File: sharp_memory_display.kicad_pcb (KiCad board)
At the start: 2 copper layers, 34.2 x 22.4 mm, 20 parts, among them J1 Conn_01x05, J2 Conn_01x10, J3 Conn_01x05_Male, J4 Conn_01x10

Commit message: simplified version
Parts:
- removed H1, H2, H3, H4: MountingHole, MountingHole:MountingHole_2.2mm_M2_DIN965_Pad
- removed J4: Conn_01x10, Connector_FFC-FPC:Hirose_FH12-10S-0.5SH_1x10-1MP_P0.50mm_Horizontal
- removed REF** (x4): breakaway-mousebites-three, Keebio-Parts:breakaway-mousebites-three
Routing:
- net EXTMODE: track 24.9 -> 9.01 mm, vias 3 -> 2
- net VSSA: track 26.6 -> 11.0 mm, vias 1 -> 0
- net VDDA: track 27.1 -> 12.1 mm, vias 1 -> 0
- net DISP: track 20.5 -> 6.77 mm, vias 1 -> 0
- net EXTCOMIN: track 21.2 -> 8.33 mm, vias 1 -> 0
- net SCLK: track 33.2 -> 26.5 mm, vias 1 -> 0
- net SCS: track 31.5 -> 25.6 mm, vias 1 -> 0
- net VDD: track 46.8 -> 42.9 mm
- net VSS: track 48.3 -> 44.5 mm
- net SI: track 39.5 -> 36.0 mm
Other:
- board size 34.2 x 22.4 mm -> 34.2 x 14 mm

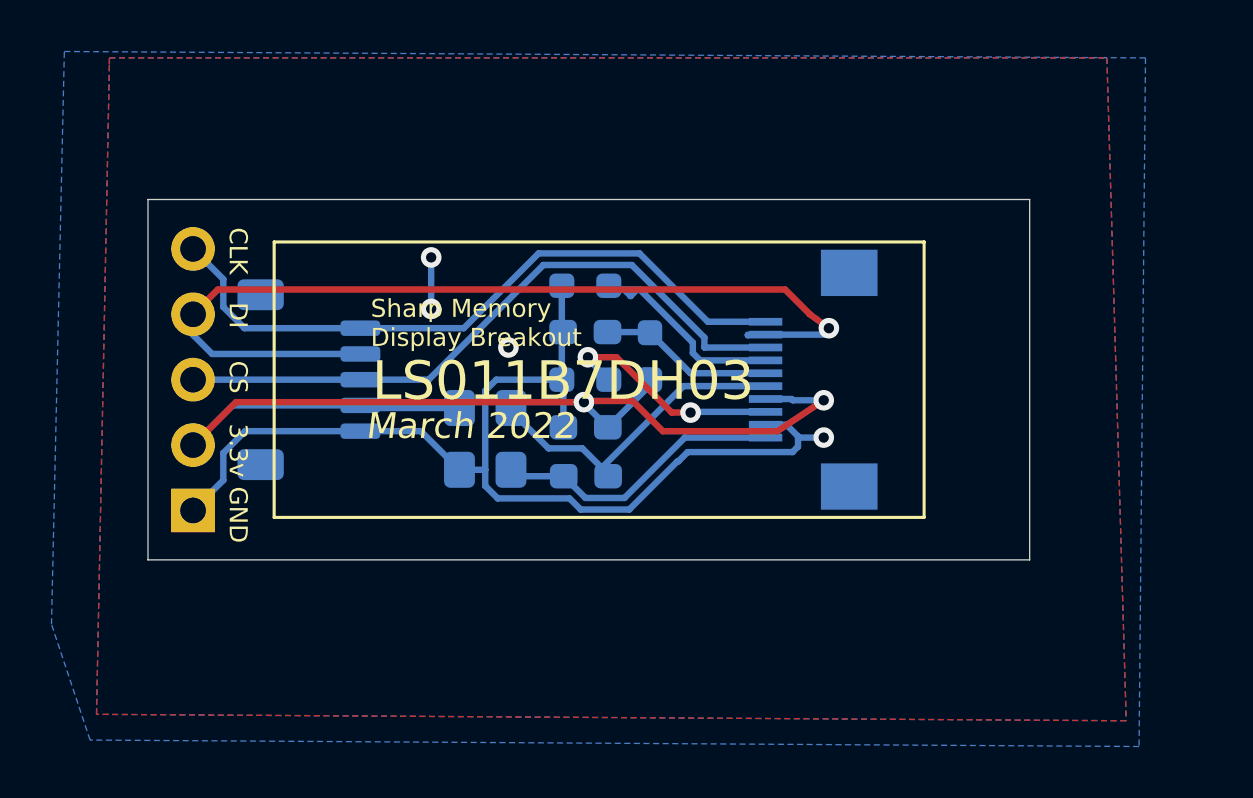
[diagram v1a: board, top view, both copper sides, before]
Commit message: add two extra pint sockets
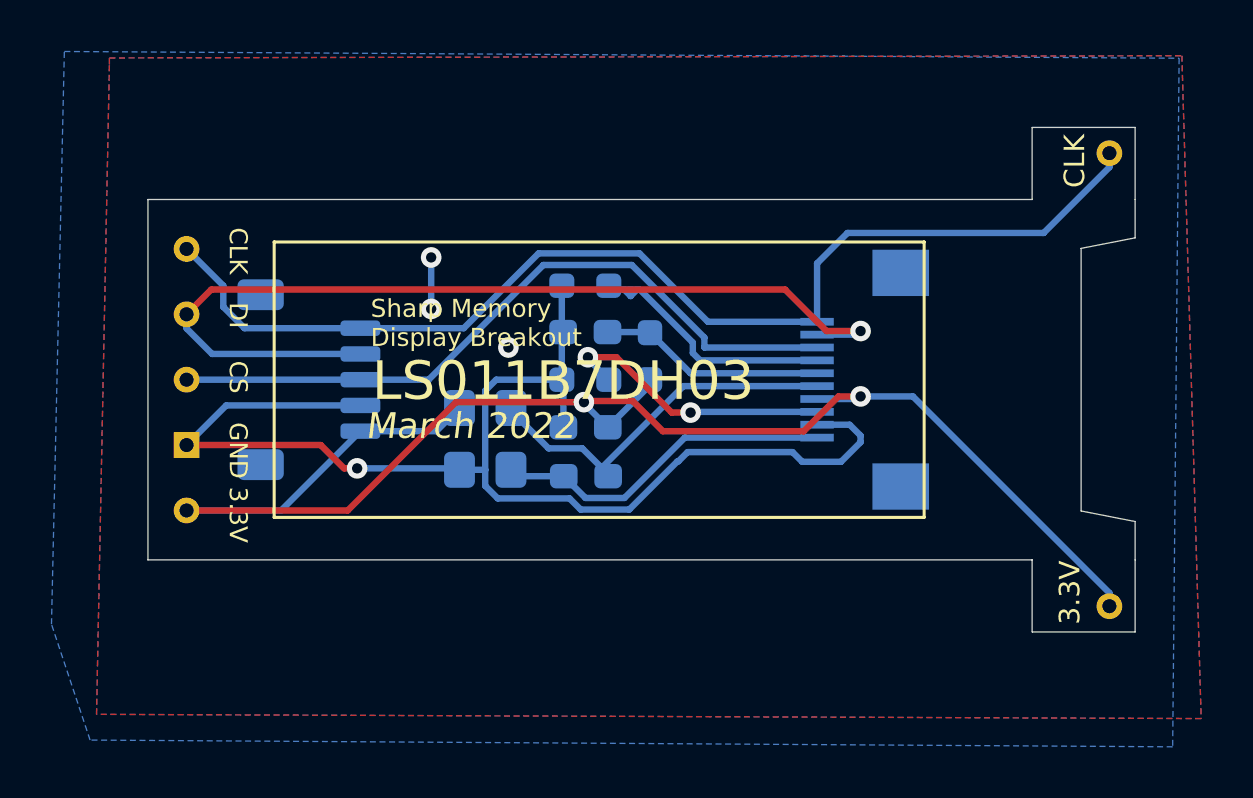
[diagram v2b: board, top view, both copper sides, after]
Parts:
- added J4: Conn_01x01_Female, Connector_PinSocket_2.54mm:PinSocket_1x01_P2.54mm_Vertical, F.Cu at (59.9, 21.7)
- added J5: Conn_01x01_Female, Connector_PinSocket_2.54mm:PinSocket_1x01_P2.54mm_Vertical, F.Cu at (59.9, 39.3)
- moved J2 2.00 mm to (54.9, 30.5)
- moved J1 0.25 mm to (24.0, 35.6)
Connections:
- J1 pad 1: VSS -> VDD
- J1 pad 2: VDD -> VSS
- J3 pad 1: VSS -> VDD
- J3 pad 2: VDD -> VSS
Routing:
- net SCLK: track 26.5 -> 44.3 mm
- net VDD: track 42.9 -> 60.0 mm
- net VSS: track 44.5 -> 52.1 mm
- net SCS: track 25.6 -> 27.9 mm
- net VSSA: track 11.0 -> 13.0 mm
- net EXTMODE: track 9.01 -> 11.0 mm
- net EXTCOMIN: track 8.33 -> 10.3 mm
- net DISP: track 6.77 -> 8.77 mm
- net VDDA: track 12.1 -> 14.1 mm
- net SI: track 36.0 -> 36.7 mm
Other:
- board size 34.2 x 14 mm -> 38.4 x 19.6 mm
